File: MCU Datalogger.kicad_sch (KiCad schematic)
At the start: 25 parts, among them U1 24LC1025, U2 24LC1025, U3 DS1337S_, U4 ATMEGA328P-AU, Y1 16 MHz, Y2 32.768 kHZ

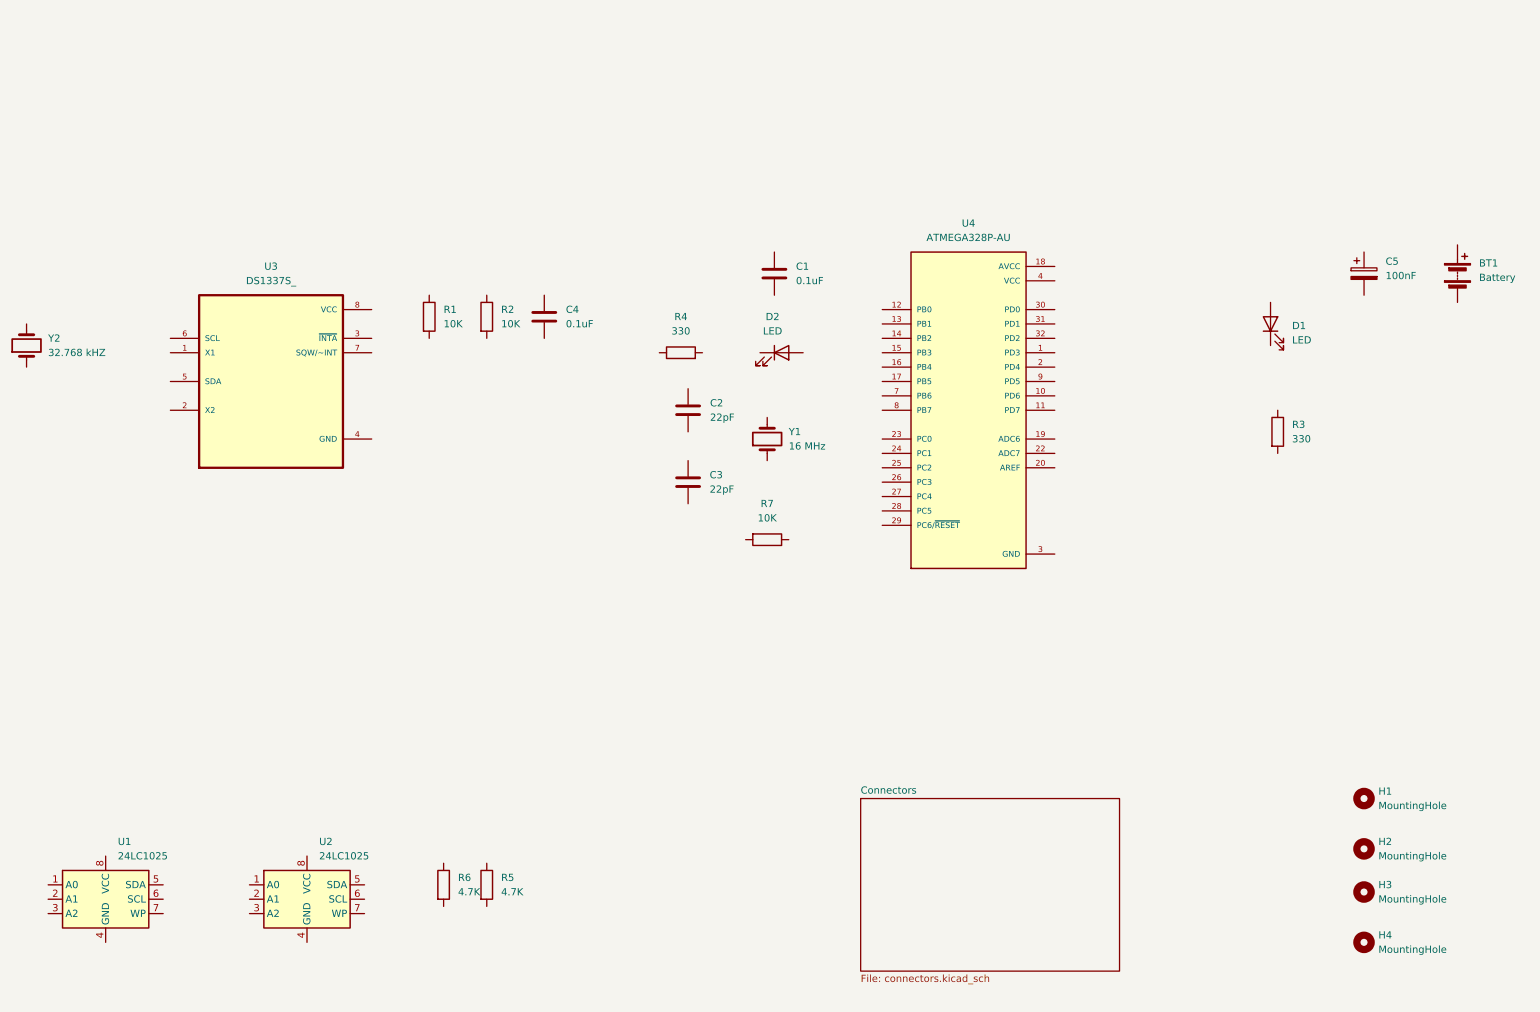
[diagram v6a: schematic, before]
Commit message: Completed wiring of sheet
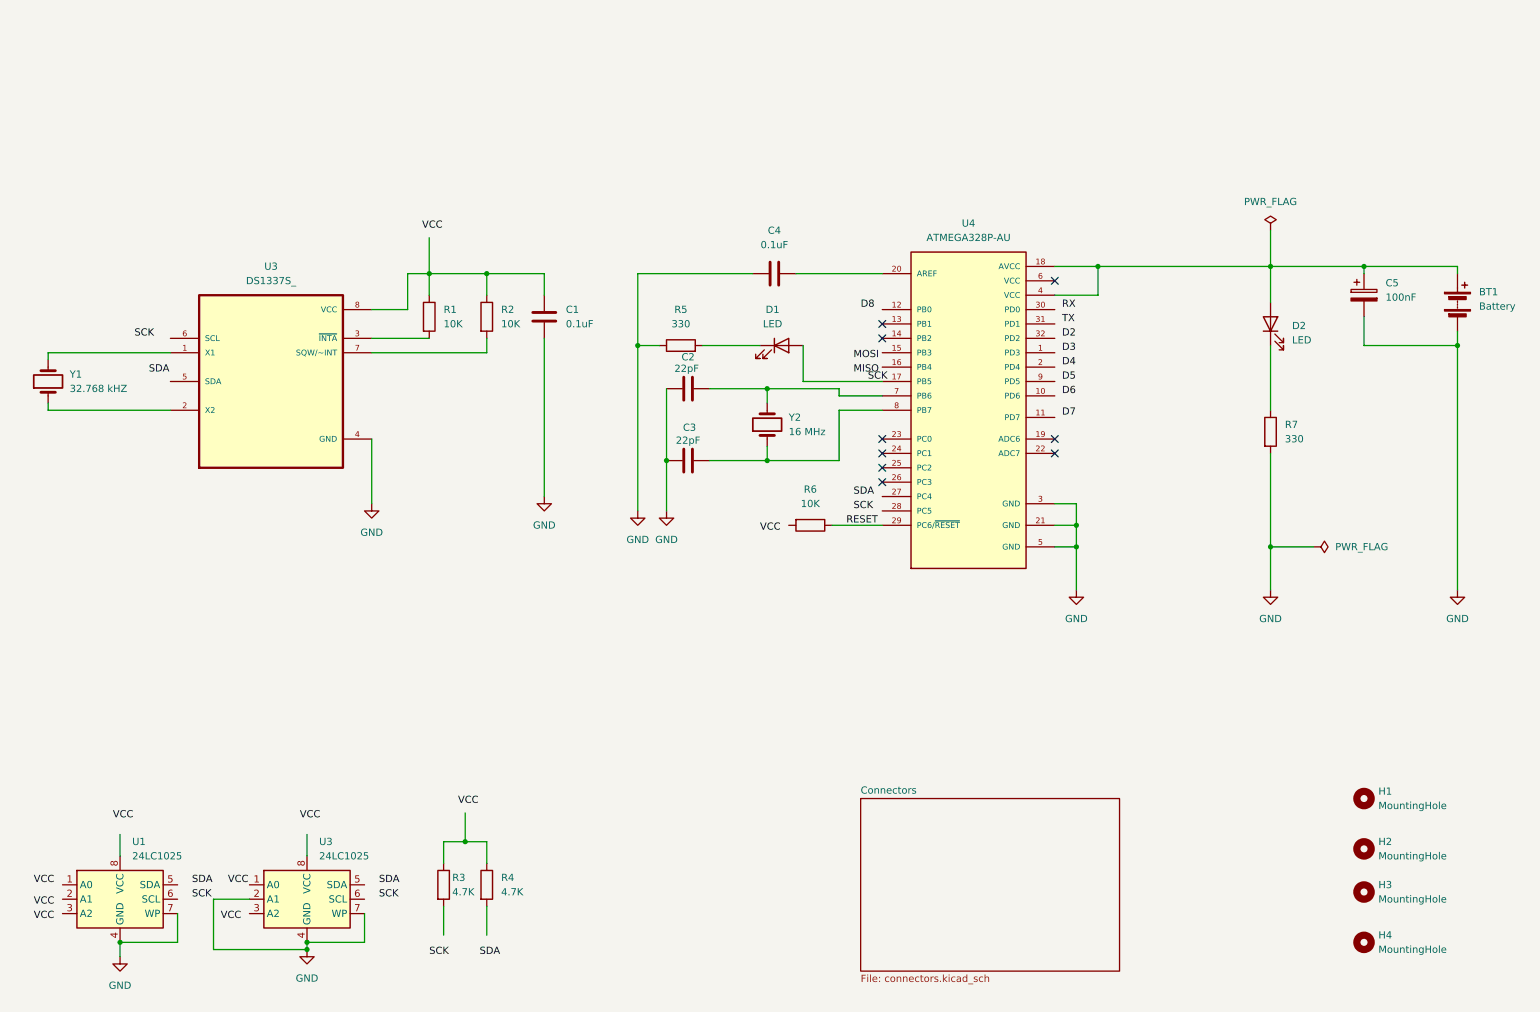
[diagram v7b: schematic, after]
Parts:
- U4: Availability In Stock -> (none); Check_prices https://www.snapeda.com/parts/ATMEGA328P-AU/Microchip+Techn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 -> (none); MAXIMUM_PACKAGE_HEIGHT 1.20mm -> (none); Package TQFP-32 Microchip -> (none); Price None -> (none); Purchase-URL https://www.snapeda.com/api/url_track_click_mouser/?unipart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 -> (none); STANDARD IPC-7351B -> (none); SnapEDA_Link https://www.snapeda.com/parts/ATMEGA328P-AU/Microchip+Techn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 -> (none)
- renumbered C4 to C1, C1 to C4, D2 to D1, D1 to D2, R6 to R3, R5 to R4, R4 to R5, R7 to R6, R3 to R7, U2 to U3, Y2 to Y1, Y1 to Y2
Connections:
- net GND: now also BT1.2 (-), C1.2, C2.1, C3.1, C4.1, C5.2, R5.1, R7.2, U1.4 (GND), U1.7 (WP), U3.2 (A1), U3.4 (GND), U3.4 (GND), U3.7 (WP)
- net VCC: no longer U4.4 (VCC), U4.6 (VCC)
- net at Y1.1: now also U3.2 (X2)
- net at Y1.2: now also U3.1 (X1)
- net at R2.1: now also C1.1, R1.1, U3.8 (VCC)
- net at R2.2: now also U3.7 (SQW/~INT)
- net at R1.2: now also U3.3 (~{INTA})
- net at R4.1: now also R3.1
- net at C5.1: now also BT1.1 (+), D2.2 (A), U4.18 (AVCC), U4.4 (VCC)
- net at C4.2: now also U4.20 (AREF)
- net RESET: now reaches R6.1
- net RESET: now also U4.29 (PC6/~{RESET})
- net at Y2.1: now also C3.2, U4.8 (PB7)
- net at Y2.2: now also C2.2, U4.7 (PB6)
- net at D1.1 (K): now also R5.2
- net SCK: now reaches D1.2 (A)
- net SCK: now also U4.17 (PB5)
- net at R7.1: now also D2.1 (K)
- no-connect marks 0 -> 9
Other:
- moved on the sheet: BT1, C2, C3, C4, C5, D1, R5, R6, R7, U1, Y1, Y2

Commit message: Completed wiring
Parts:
- renumbered U3 to U2
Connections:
- net D2: now also U4.32 (PD2)
- net D3: now also U4.1 (PD3)
- net D4: now also U4.2 (PD4)
- net D5: now also U4.9 (PD5)
- net D6: now also U4.10 (PD6)
- net D7: now also U4.11 (PD7)
- net D8: now also U4.12 (PB0)
- net MISO: now also U4.16 (PB4)
- net MOSI: now also U4.15 (PB3)
- net RX: now also U4.30 (PD0)
- net SCK: now also R3.2, U1.6 (SCL), U2.6 (SCL), U3.6 (SCL), U4.28 (PC5)
- net SDA: now also R4.2, U1.5 (SDA), U2.5 (SDA), U3.5 (SDA), U4.27 (PC4)
- net TX: now also U4.31 (PD1)
- net VCC: now also C1.1, R1.1, R2.1, R3.1, R4.1, R6.2, U1.1 (A0), U1.2 (A1), U1.3 (A2), U1.8 (VCC), U2.8 (VCC), U3.1 (A0), U3.3 (A2), U3.8 (VCC)
- no-connect marks 9 -> 11
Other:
- sheet Connectors ports: added D2, D3, D4, D5, D6, D7, D8, GND, MISO, MOSI, RESET, RX, SCK, SDA, TX, VCC; removed none
- moved on the sheet: R6
